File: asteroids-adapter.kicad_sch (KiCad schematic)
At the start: 21 parts, among them J1 Asteroids Connector EDAC 307-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, J2 Asteroids harness connector, J3 Audio Gain, U1 TL074

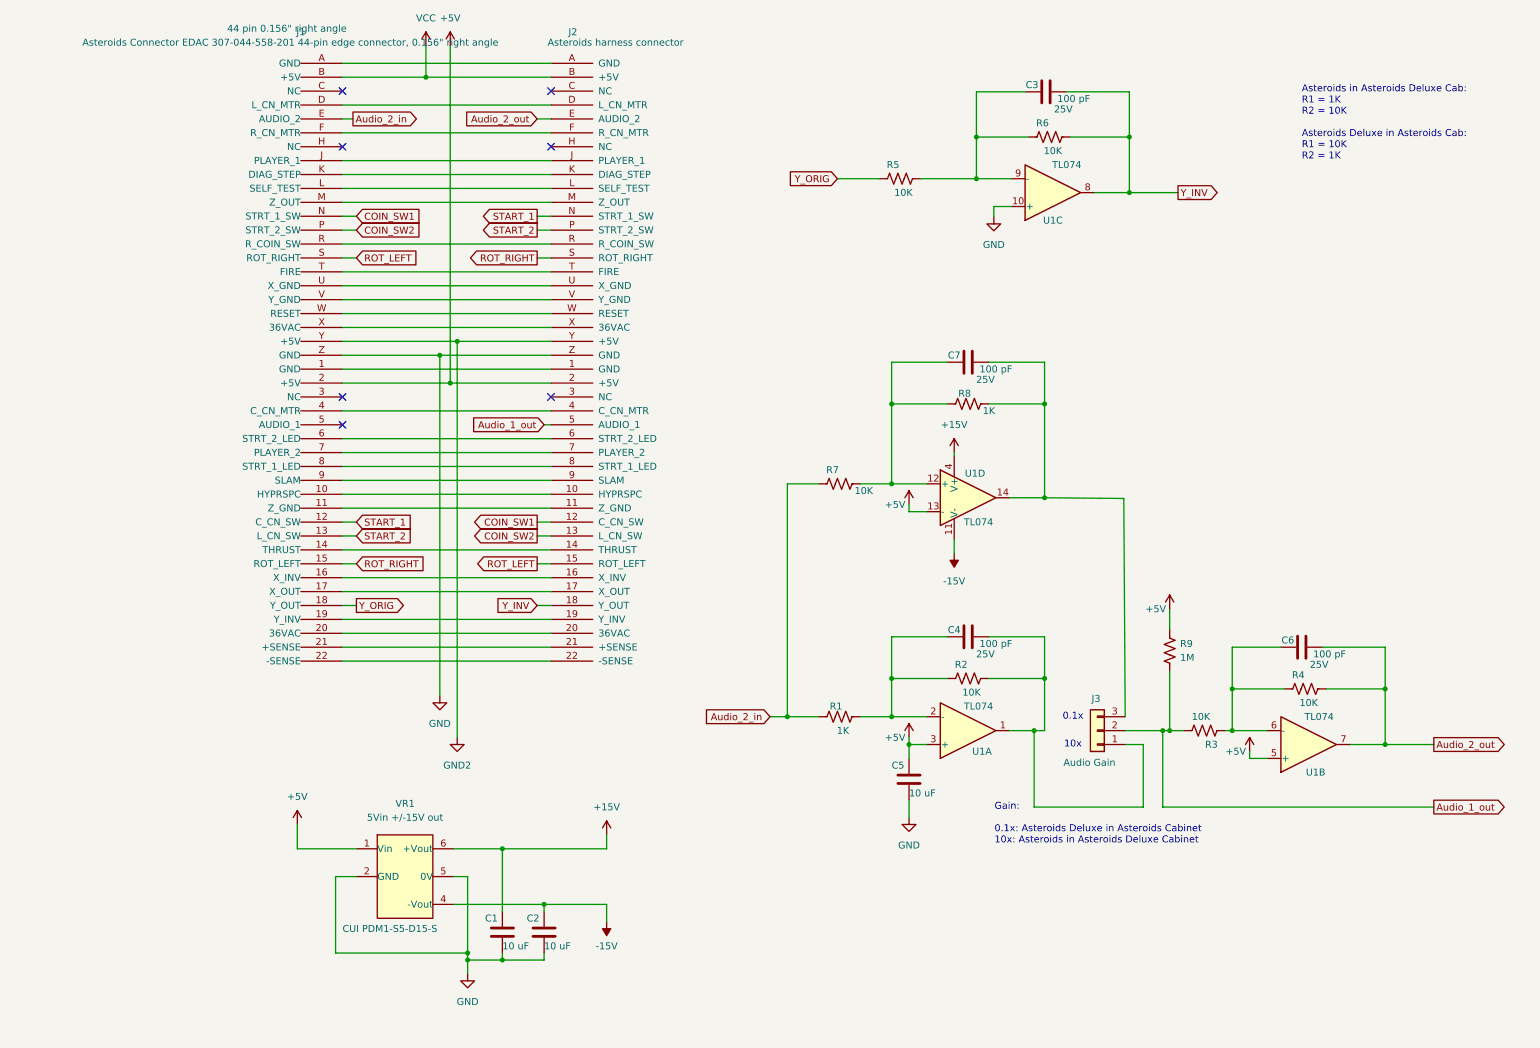
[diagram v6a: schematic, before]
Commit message: Added FLIP Y jumper
FLIP Y provides required for AST Deluxe in AST cab, and also for
Asteroids in a Deluxe cabaret cabinet.

Added 2-pin header to library

More makefile tweaks.
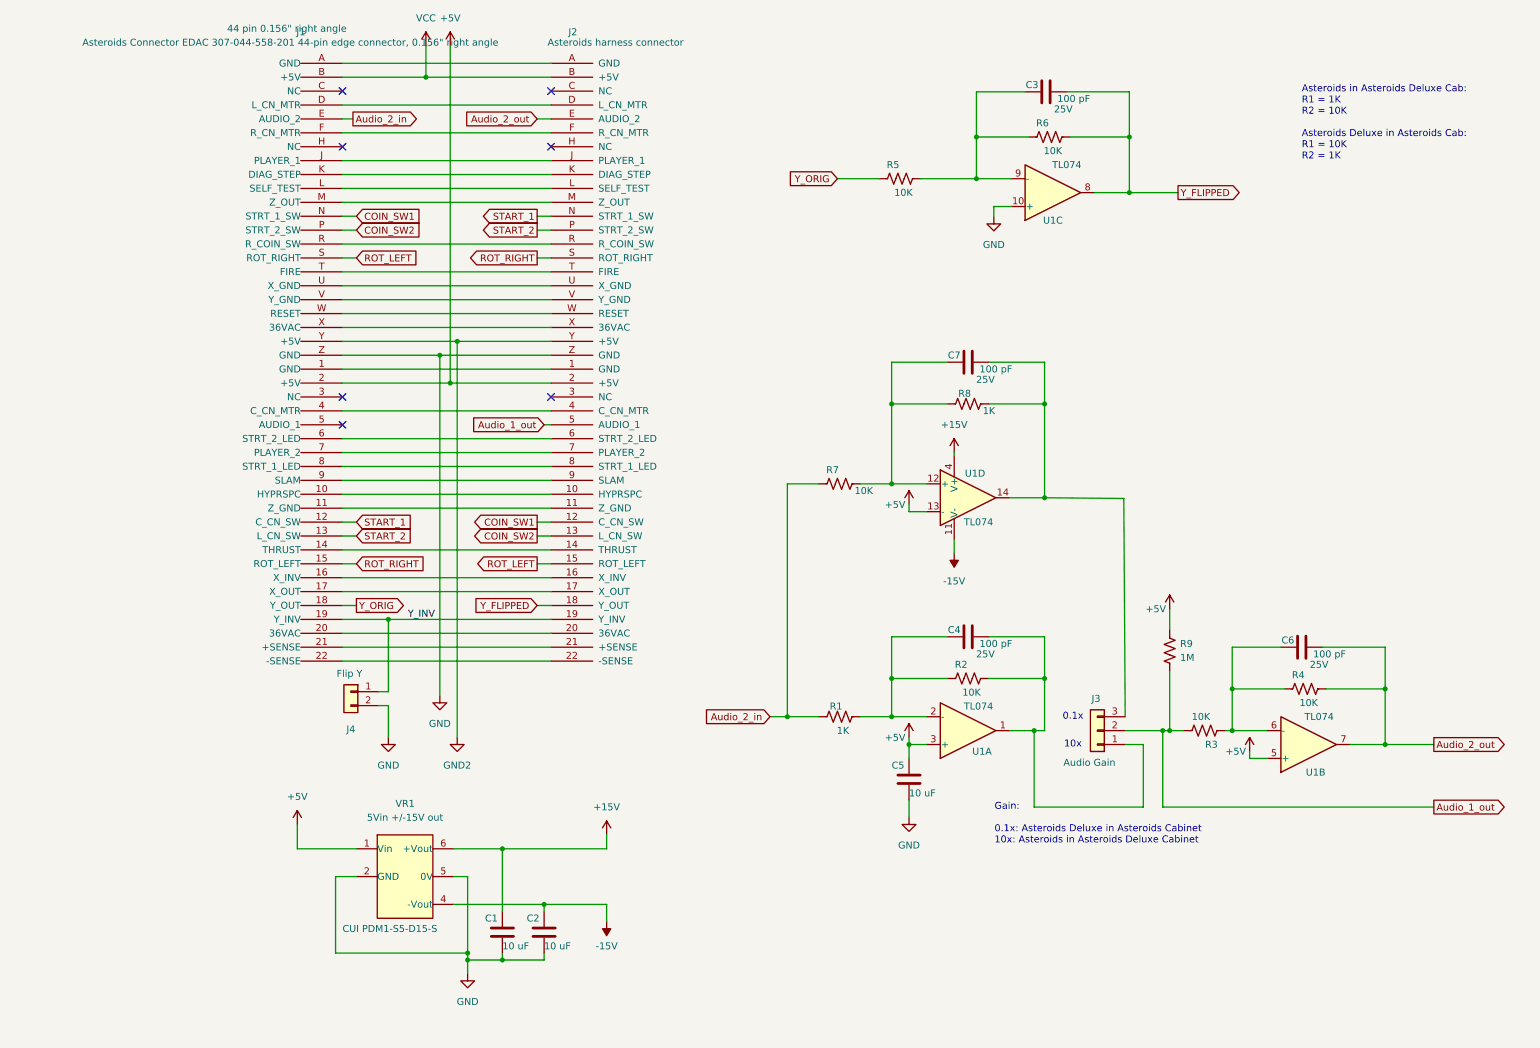
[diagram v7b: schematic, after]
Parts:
- added J4: 3M 2302-6111TG 2-pin 0.1" header, Connector_PinHeader_2.54mm:PinHeader_1x02_P2.54mm_Vertical, symbol ast-adapter:3M 2302-6111TG 2-pin 0.1{dblquote} header
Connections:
- net GND: now also J4.2 (Pin_2)
- net Y_INV: now also J1.19 (Y_INV), J2.19 (Y_INV), J4.1 (Pin_1); no longer C3.2, J2.18 (Y_OUT), R6.1, U1.8
- new net Y_FLIPPED: C3.2, J2.18 (Y_OUT), R6.1, U1.8
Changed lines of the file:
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@@
   (junction (at 237.49 137.16) (diameter 0) (color 0 0 0 0)
   )
+  (junction (at 55.372 124.46) (diameter 0) (color 0 0 0 0)
+  )
   (junction (at 196.85 144.78) (diameter 0) (color 0 0 0 0)
   )
@@
     (stroke (width 0) (type default) (color 0 0 0 0))
   )
+  (wire (pts (xy 55.372 140.208) (xy 55.372 146.05))
+    (stroke (width 0) (type default) (color 0 0 0 0))
+  )
   (wire (pts (xy 46.99 111.76) (xy 85.09 111.76))
     (stroke (width 0) (type default) (color 0 0 0 0))
@@
     (stroke (width 0) (type default) (color 0 0 0 0))
   )
+  (wire (pts (xy 55.372 124.46) (xy 85.09 124.46))
+    (stroke (width 0) (type default) (color 0 0 0 0))
+  )
   (wire (pts (xy 179.959 36.322) (xy 190.754 36.322))
     (stroke (width 0) (type default) (color 0 0 0 0))
@@
     (stroke (width 0) (type default) (color 0 0 0 0))
   )
+  (wire (pts (xy 55.372 137.668) (xy 53.594 137.668))
+    (stroke (width 0) (type default) (color 0 0 0 0))
+  )
   (wire (pts (xy 83.82 176.53) (xy 95.25 176.53))
     (stroke (width 0) (type default) (color 0 0 0 0))
@@
     (stroke (width 0) (type default) (color 0 0 0 0))
   )
+  (wire (pts (xy 55.372 124.46) (xy 55.372 137.668))
+    (stroke (width 0) (type default) (color 0 0 0 0))
+  )
   (wire (pts (xy 147.32 135.255) (xy 157.48 135.255))
     (stroke (width 0) (type default) (color 0 0 0 0))
@@
     (stroke (width 0) (type default) (color 0 0 0 0))
   )
+  (wire (pts (xy 53.594 140.208) (xy 55.372 140.208))
+    (stroke (width 0) (type default) (color 0 0 0 0))
+  )
   (wire (pts (xy 147.32 77.47) (xy 147.32 85.09))
     (stroke (width 0) (type default) (color 0 0 0 0))
@@
     (stroke (width 0) (type default) (color 0 0 0 0))
   )
-  (wire (pts (xy 46.99 124.46) (xy 85.09 124.46))
+  (wire (pts (xy 46.99 124.46) (xy 55.372 124.46))
     (stroke (width 0) (type default) (color 0 0 0 0))
   )
@@
     (effects (font (size 1.27 1.27)) (justify left bottom))
   )
+  (label "Y_INV" (at 58.928 124.46 0)
+    (effects (font (size 1.27 1.27)) (justify left bottom))
+  )
   (global_label "Audio_1_out" (shape output) (at 246.38 158.75 0) (fields_autoplaced)
     (effects (font (size 1.27 1.27)) (justify left))
@@
     )
   )
-  (global_label "Y_INV" (shape input) (at 82.55 121.92 180) (fields_autoplaced)
+  (global_label "Y_FLIPPED" (shape input) (at 82.55 121.92 180) (fields_autoplaced)
     (effects (font (size 1.27 1.27)) (justify right))
-    (property "Intersheet References" "${INTERSHEET_REFS}" (id 0) (at 75.0569 121.9994 0)
+    (property "Intersheet References" "${INTERSHEET_REFS}" (id 0) (at 70.4002 121.8406 0)
       (effects (font (size 1.27 1.27)) (justify right) hide)
     )
@@
     )
   )
-  (global_label "Y_INV" (shape output) (at 199.644 46.482 0) (fields_autoplaced)
+  (global_label "Y_FLIPPED" (shape output) (at 199.644 46.482 0) (fields_autoplaced)
     (effects (font (size 1.27 1.27)) (justify left))
-    (property "Intersheet References" "${INTERSHEET_REFS}" (id 0) (at 207.1371 46.5614 0)
+    (property "Intersheet References" "${INTERSHEET_REFS}" (id 0) (at 211.7938 46.4026 0)
       (effects (font (size 1.27 1.27)) (justify left) hide)
     )
@@
     (pin "1")
   )
+  (symbol (lib_id "ast-adapter:3M  2302-6111TG  2-pin 0.1{dblquote} header") (at 53.594 137.668 0) (mirror y) (unit 1)
+    (in_bom yes) (on_board yes)
+    (property "Reference" "J4" (id 0) (at 48.514 144.526 0))
+    (property "Value" "3M  2302-6111TG  2-pin 0.1\" header" (id 1) (at 81.534 172.466 0)
+      (effects (font (size 1.27 1.27)) (justify left) hide)
+    )
+    (property "Footprint" "Connector_PinHeader_2.54mm:PinHeader_1x02_P2.54mm_Vertical" (id 2) (at 52.6288 141.478 0)
+      (effects (font (size 1.27 1.27)) hide)
+    )
+    (property "Datasheet" "https://multimedia.3m.com/mws/media/22434O/3mtm-100-in-pin-strip-hdr-straight-ra-solder-tail-ts0766.pdf&fn=ts0766.pdf" (id 3) (at 79.756 167.132 0)
+      (effects (font (size 1.27 1.27)) hide)
+    )
+    (property "Component Value" "Flip Y" (id 4) (at 48.26 134.366 0))
+    (property "Tolerance" "If applicable" (id 5) (at 75.692 177.292 0)
+      (effects (font (size 1.27 1.27)) hide)
+    )
+    (property "Manufacturer" "3M" (id 6) (at 79.756 155.956 0)
+      (effects (font (size 1.27 1.27)) hide)
+    )
+    (property "Manufacturer Link" "https://www.mouser.com/ProductDetail/3M-Electronic-Solutions-Division/2303-6111TG?qs=r3lCeSWZErXCf6CgpVZt0A%3D%3D" (id 7) (at 76.962 162.56 0)
+      (effects (font (size 1.27 1.27)) hide)
+    )
+    (property "RoHS Document Link" "https://multimedia.3m.com/mws/media/22434O/3mtm-100-in-pin-strip-hdr-straight-ra-solder-tail-ts0766.pdf&fn=ts0766.pdf" (id 8) (at 76.708 202.438 0)
+      (effects (font (size 1.27 1.27)) hide)
+    )
+    (property "Manufacturer PN" "2302-6111TG" (id 9) (at 77.47 159.512 0)
+      (effects (font (size 1.27 1.27)) hide)
+    )
+    (property "RoHS" "Yes" (id 10) (at 80.01 199.644 0)
+      (effects (font (size 1.27 1.27)) hide)
+    )
+    (property "Allow Substitution" "Yes" (id 11) (at 80.264 205.486 0)
+      (effects (font (size 1.27 1.27)) hide)
+    )
+    (property "Fitted" "Yes" (id 12) (at 79.248 210.312 0)
+      (effects (font (size 1.27 1.27)) hide)
+    )
+    (property "Tracking" "No" (id 13) (at 79.756 207.772 0)
+      (effects (font (size 1.27 1.27)) hide)
+    )
+    (property "BOM Comment" "" (id 14) (at 53.594 137.668 0)
+      (effects (font (size 1.27 1.27)) hide)
+    )
+    (property "Component Type" "pin header" (id 15) (at 58.166 174.498 0)
+      (effects (font (size 1.27 1.27)) hide)
+    )
+    (property "Package Type" "" (id 16) (at 53.594 137.668 0)
+      (effects (font (size 1.27 1.27)) hide)
+    )
+    (property "Package Variant" "" (id 17) (at 53.594 137.668 0)
+      (effects (font (size 1.27 1.27)) hide)
+    )
+    (property "Number of Pins" "2" (id 18) (at 75.692 179.832 0)
+      (effects (font (size 1.27 1.27)) hide)
+    )
+    (property "Temp (Storage)" "standard" (id 19) (at 75.692 181.864 0)
+      (effects (font (size 1.27 1.27)) hide)
+    )
+    (property "Temp (Operating)" "-55C/+105C" (id 20) (at 75.438 184.404 0)
+      (effects (font (size 1.27 1.27)) hide)
+    )
+    (property "Temp (Soldering)" "standard" (id 21) (at 75.438 187.198 0)
+      (effects (font (size 1.27 1.27)) hide)
+    )
+    (property "Current Rating" "3A" (id 22) (at 75.438 192.278 0)
+      (effects (font (size 1.27 1.27)) hide)
+    )
+    (property "Material" "Cu alloy / glass-filled thermoplastic" (id 23) (at 75.438 194.564 0)
+      (effects (font (size 1.27 1.27)) hide)
+    )
+    (property "Standards Version" "1.1" (id 24) (at 79.248 213.36 0)
+      (effects (font (size 1.27 1.27)) hide)
+    )
+    (pin "1")
+    (pin "2")
+  )
   (symbol (lib_id "ast-adapter:TL074") (at 161.29 102.235 0) (unit 4)
     (in_bom yes) (on_board yes)
@@
     (pin "1")
   )
+  (symbol (lib_id "power:GND") (at 55.372 146.05 0) (unit 1)
+    (in_bom yes) (on_board yes) (fields_autoplaced)
+    (property "Reference" "#PWR0116" (id 0) (at 55.372 152.4 0)
+      (effects (font (size 1.27 1.27)) hide)
+    )
+    (property "Value" "GND" (id 1) (at 55.372 151.13 0))
+    (property "Footprint" "" (id 2) (at 55.372 146.05 0)
+      (effects (font (size 1.27 1.27)) hide)
+    )
+    (property "Datasheet" "" (id 3) (at 55.372 146.05 0)
+      (effects (font (size 1.27 1.27)) hide)
+    )
+    (pin "1")
+  )
   (symbol (lib_id "ast-adapter:Yageo 1Mohm 1% thin film TH_1") (at 198.12 130.175 90) (unit 1)
     (in_bom yes) (on_board yes) (fields_autoplaced)
@@
       (reference "#PWR0115") (unit 1) (value "+5V") (footprint "")
     )
+    (path "/eeae0e53-d207-40ff-a634-1fc0ab4fd1bf"
+      (reference "#PWR0116") (unit 1) (value "GND") (footprint "")
+    )
     (path "/b69dd169-bf84-4046-9a1b-6643baa5defd"
       (reference "C1") (unit 1) (value "Kemet 10 uF 25V MLCC TH") (footprint "Capacitor_THT:C_Disc_D3.0mm_W1.6mm_P2.50mm")
@@
       (reference "J3") (unit 1) (value "Audio Gain") (footprint "Connector_PinHeader_2.54mm:PinHeader_1x03_P2.54mm_Vertical")
     )
+    (path "/895258b2-feb0-4bb8-9a2a-e6e208e47f94"
+      (reference "J4") (unit 1) (value "3M  2302-6111TG  2-pin 0.1\" header") (footprint "Connector_PinHeader_2.54mm:PinHeader_1x02_P2.54mm_Vertical")
+    )
     (path "/185bf6d4-58a9-4404-a9bd-baa7ca32e3cd"

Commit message: More cleanups and bump version
- Cleaned up schematic to align components to grid

- Added bypass cap on 0.1x gain input

- More Makefile cleanups
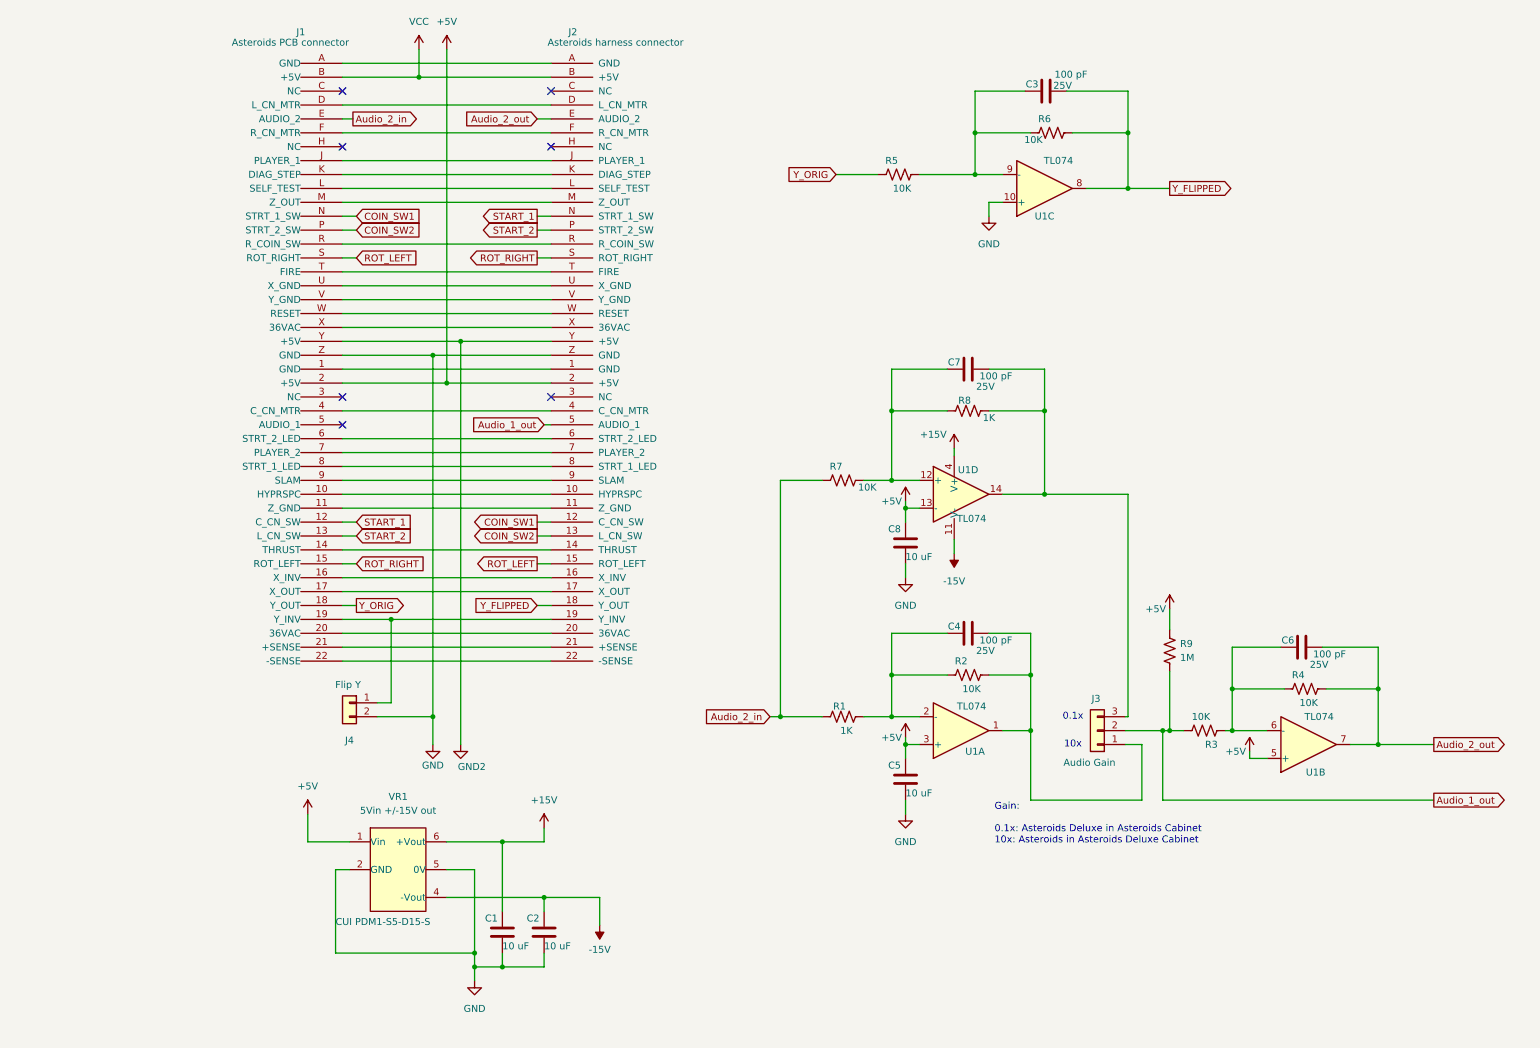
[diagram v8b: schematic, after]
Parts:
- added C8: Kemet 10 uF 25V MLCC TH, Capacitor_THT:C_Disc_D3.0mm_W1.6mm_P2.50mm, symbol ast-adapter:Kemet 10 uF 25V MLCC TH
- J1: value Asteroids Connector EDAC 307-044-558-201 44-pin edge connector, 0.156" right angle -> Asteroids PCB connector
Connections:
- net +5V: now also C8.2
- net GND: now also C8.1
- net Y_INV: no longer names the net of J1.19 (Y_INV), J2.19 (Y_INV), J4.1 (Pin_1)
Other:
- note removed: "Asteroids in Asteroids Deluxe Cab: R1 = 1K R2 = 10K Asteroids Deluxe in Asteroids Cab: R1 = 10K R2 = 1K"
- moved on the sheet: C4, C5, C7, J4, R1, R2, R5, R6, R7, R8, U1A, U1C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
